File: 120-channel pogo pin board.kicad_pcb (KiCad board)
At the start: 2 copper layers, 75 x 50 mm, 241 parts, among them P1 CONN_1, P10 CONN_1, P100 CONN_1, P101 CONN_1, P102 CONN_1, P103 CONN_1, P104 CONN_1, P105 CONN_1, P106 CONN_1, P107 CONN_1, P108 CONN_1, P109 CONN_1, P11 CONN_1, P110 CONN_1, P111 CONN_1, P112 CONN_1, P113 CONN_1, P114 CONN_1, P115 CONN_1, P116 CONN_1, P117 CONN_1, P118 CONN_1, P119 CONN_1, P12 CONN_1, P120 CONN_1, P121 CONN_1, P13 CONN_1, P14 CONN_1, P15 CONN_1, P16 CONN_1, P17 CONN_1, P18 CONN_1, P19 CONN_1, P2 CONN_1, P20 CONN_1, P21 CONN_1, P22 CONN_1, P23 CONN_1, P24 CONN_1, P25 CONN_1, P26 CONN_1, P27 CONN_1, P28 CONN_1, P29 CONN_1, P3 CONN_1, P30 CONN_1, P31 CONN_1, P32 CONN_1, P33 CONN_1, P34 CONN_1, P35 CONN_1, P36 CONN_1, P37 CONN_1, P38 CONN_1, P39 CONN_1, P4 CONN_1, P40 CONN_1, P41 CONN_1, P42 CONN_1, P43 CONN_1, P44 CONN_1, P45 CONN_1, P46 CONN_1, P47 CONN_1, P48 CONN_1, P49 CONN_1, P5 CONN_1, P50 CONN_1, P51 CONN_1, P52 CONN_1, P53 CONN_1, P54 CONN_1, P55 CONN_1, P56 CONN_1, P57 CONN_1, P58 CONN_1, P59 CONN_1, P6 CONN_1, P60 CONN_1, P61 CONN_1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

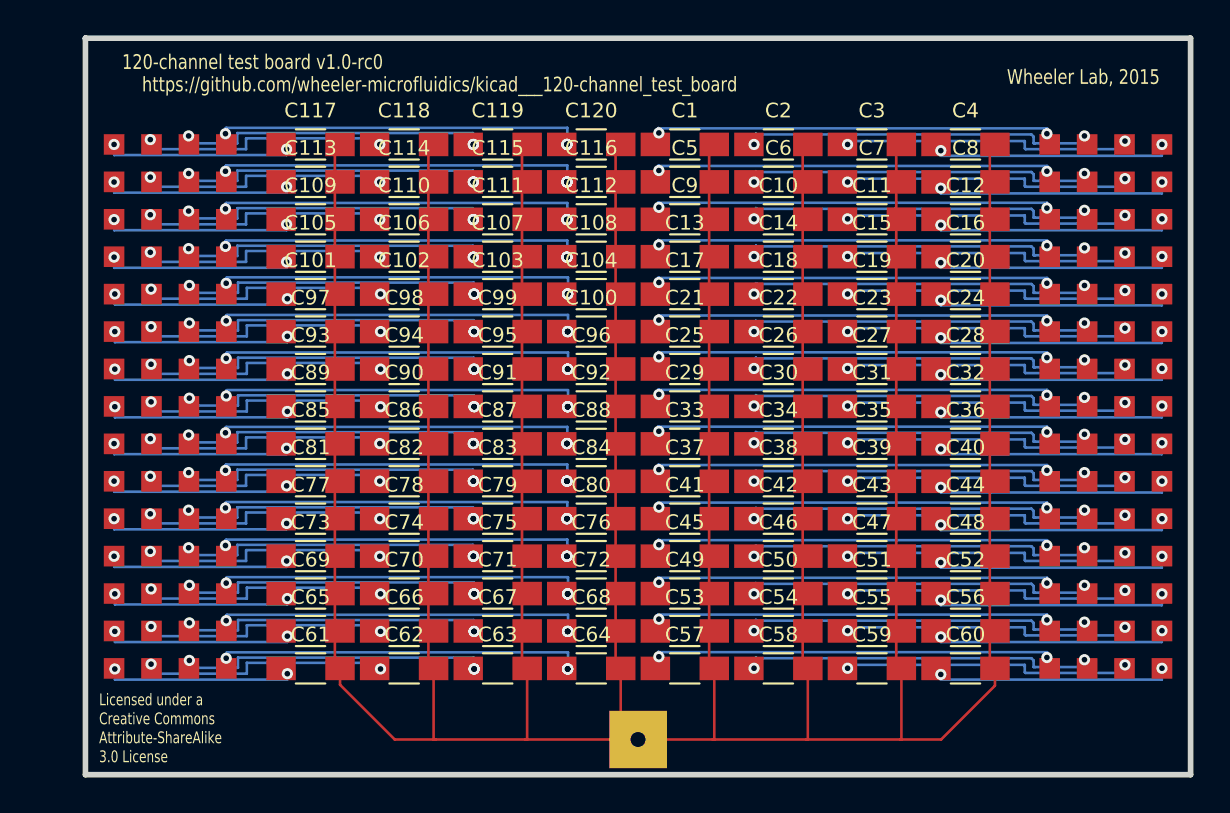
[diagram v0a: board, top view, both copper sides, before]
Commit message: Update for compatibility with DropBot v3
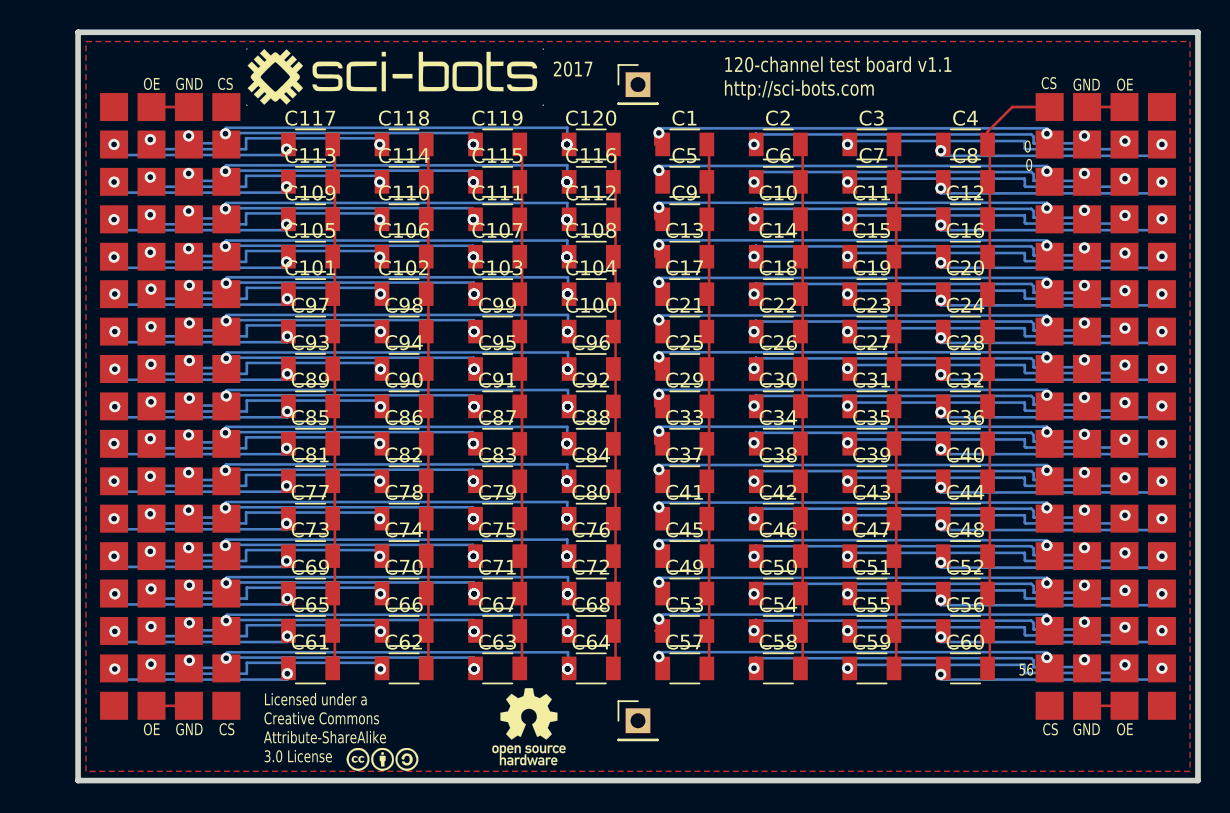
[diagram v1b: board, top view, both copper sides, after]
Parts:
- added G***: LOGO, WheelerLab:SCI-BOTS-LOGO, F.Cu at (59.7, 38.6)
- added G***: LOGO, WheelerLab:CC_S_A_logo_5mm, F.Cu at (58.9, 84.9)
- added G***: LOGO, WheelerLab:OSHW_logo_5mm, F.Cu at (68.8, 82.7)
- added P122: CONN_01X01, wheelerlab:1.9mm_DMF_Electrode, F.Cu at (48.3, 40.6)
- added P123: CONN_01X01, wheelerlab:1.9mm_DMF_Electrode, F.Cu at (48.3, 81.3)
- added P124: CONN_01X01, wheelerlab:1.9mm_DMF_Electrode, F.Cu at (104.1, 81.3)
- added P125: CONN_01X01, wheelerlab:1.9mm_DMF_Electrode, F.Cu at (104.1, 40.6)
- added P126: CONN_01X01, wheelerlab:1.9mm_DMF_Electrode, F.Cu at (45.7, 40.6)
- added P127: CONN_01X01, wheelerlab:1.9mm_DMF_Electrode, F.Cu at (43.2, 40.6)
- added P128: CONN_01X01, wheelerlab:1.9mm_DMF_Electrode, F.Cu at (45.7, 81.3)
- added P129: CONN_01X01, wheelerlab:1.9mm_DMF_Electrode, F.Cu at (43.2, 81.3)
- added P130: CONN_01X01, wheelerlab:1.9mm_DMF_Electrode, F.Cu at (106.7, 81.3)
- added P131: CONN_01X01, wheelerlab:1.9mm_DMF_Electrode, F.Cu at (109.2, 81.3)
- added P132: CONN_01X01, wheelerlab:1.9mm_DMF_Electrode, F.Cu at (106.7, 40.6)
- added P133: CONN_01X01, wheelerlab:1.9mm_DMF_Electrode, F.Cu at (109.2, 40.6)
- added P134: CONN_01X01, wheelerlab:1.9mm_DMF_Electrode, F.Cu at (40.6, 40.6)
- added P135: CONN_01X01, wheelerlab:1.9mm_DMF_Electrode, F.Cu at (40.6, 81.3)
- added P136: CONN_01X01, wheelerlab:1.9mm_DMF_Electrode, F.Cu at (111.8, 81.3)
- added P137: CONN_01X01, wheelerlab:1.9mm_DMF_Electrode, F.Cu at (111.8, 40.6)
- added P138: CONN_01X01, Pin_Headers:Pin_Header_Straight_1x01_Pitch2.54mm, F.Cu at (76.2, 39.1)
- C1, C10, C100, C101, C102, C103, C104, C105, C106, C107, C108, C109, C11, C110, C111, C112, C113, C114, C115, C116, C117, C118, C119, C12, C120, C13, C14, C15, C16, C17, C18, C19, C2, C20, C21, C22, C23, C24, C25, C26, C27, C28, C29, C3, C30, C31, C32, C33, C34, C35, C36, C37, C38, C39, C4, C40, C41, C42, C43, C44, C45, C46, C47, C48, C49, C5, C50, C51, C52, C53, C54, C55, C56, C57, C58, C59, C6, C60, C61, C62, C63, C64, C65, C66, C67, C68, C69, C7, C70, C71, C72, C73, C74, C75, C76, C77, C78, C79, C8, C80, C81, C82, C83, C84, C85, C86, C87, C88, C89, C9, C90, C91, C92, C93, C94, C95, C96, C97, C98, C99: footprint Capacitors_SMD:C_1206_HandSoldering -> Capacitors_SMD:C_1206
- P1, P10, P100, P101, P102, P103, P104, P105, P106, P107, P108, P109, P11, P110, P111, P112, P113, P114, P115, P116, P117, P118, P119, P12, P120, P13, P14, P15, P16, P17, P18, P19, P2, P20, P21, P22, P23, P24, P25, P26, P27, P28, P29, P3, P30, P31, P32, P33, P34, P35, P36, P37, P38, P39, P4, P40, P41, P42, P43, P44, P45, P46, P47, P48, P49, P5, P50, P51, P52, P53, P54, P55, P56, P57, P58, P59, P6, P60, P61, P62, P63, P64, P65, P66, P67, P68, P69, P7, P70, P71, P72, P73, P74, P75, P76, P77, P78, P79, P8, P80, P81, P82, P83, P84, P85, P86, P87, P88, P89, P9, P90, P91, P92, P93, P94, P95, P96, P97, P98, P99: value CONN_1 -> CONN_01X01; footprint wheelerlab:1.4mm_DMF_Electrode -> wheelerlab:1.9mm_DMF_Electrode
- P121: value CONN_1 -> CONN_01X01; footprint wheelerlab:3.9mm_DMF_Electrode -> Pin_Headers:Pin_Header_Straight_1x01_Pitch2.54mm
- moved P121 1.27 mm to (76.2, 82.3)
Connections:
- net Net-(C1-Pad2) renamed CUR_SENSE
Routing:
- net CUR_SENSE: track 364.4 -> 290.3 mm
- net Net-(P128-Pad1): track 0.00 -> 2.54 mm
- net Net-(P126-Pad1): track 0.00 -> 2.54 mm
- net Net-(P132-Pad1): track 0.00 -> 2.54 mm
- net Net-(P130-Pad1): track 0.00 -> 2.54 mm
- added copper zone on F.Cu, net CUR_SENSE
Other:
- board size 75 x 50 mm -> 76 x 50.8 mm
- board text added: "0"
- board text added: "120-channel test board v1.1 http://sci-bots.com"
- board text added: "2017"
- board text added: "56"
- board text added: "CS"
- board text added: "GND"
- board text added: "OE"
- board text removed: "120-channel test board v1.0-rc0"
- board text removed: "Wheeler Lab, 2015"
- board text removed: "https://github.com/wheeler-microfluidics/kicad___120-channel_test_board"
